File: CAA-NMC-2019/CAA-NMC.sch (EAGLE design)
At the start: 156 parts, among them IC1 ATTINY85-20SU, J1 M20-9980346

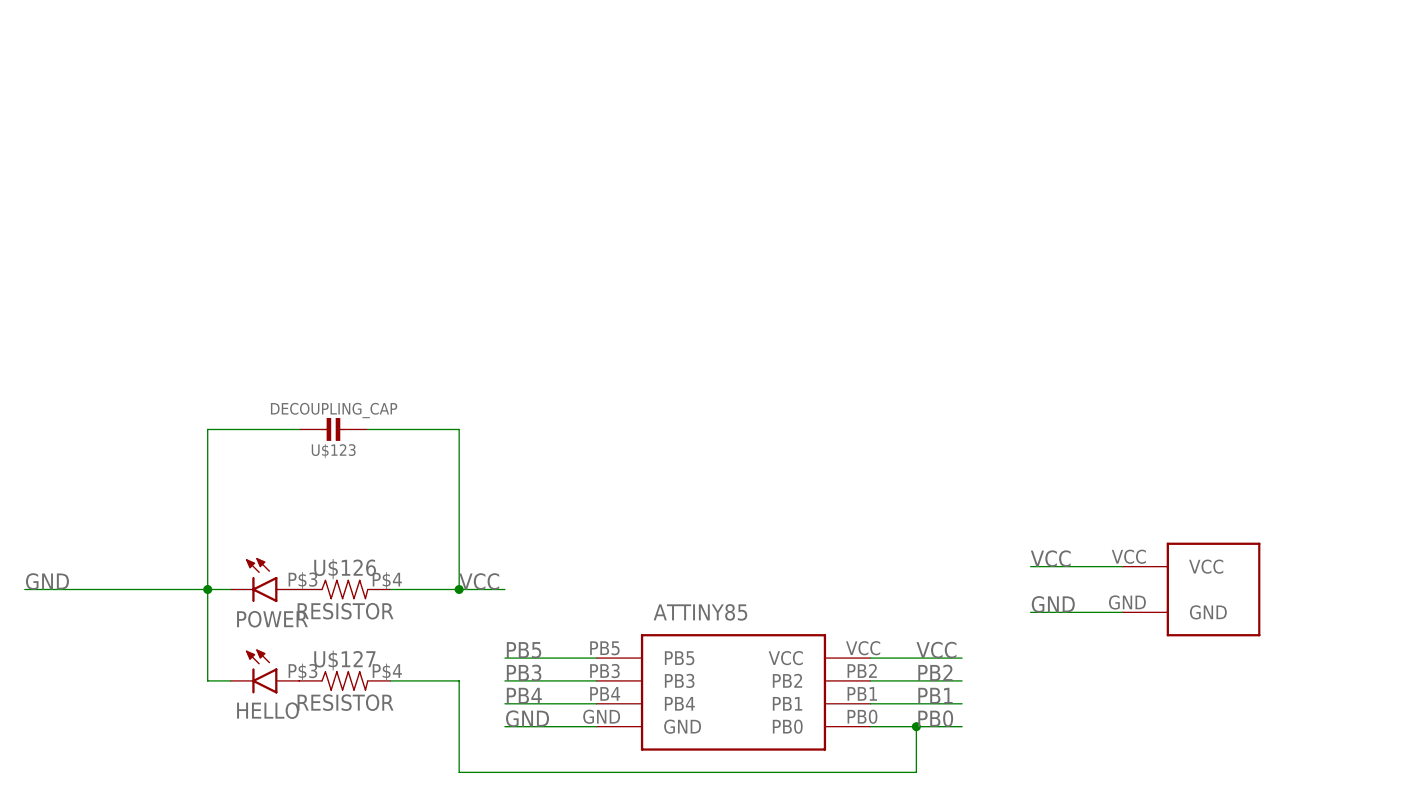
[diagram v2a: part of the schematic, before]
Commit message: added SMT switch to design/lbr
This can be used as on/off for battery, but should also be wired to isolate battery voltage from USB
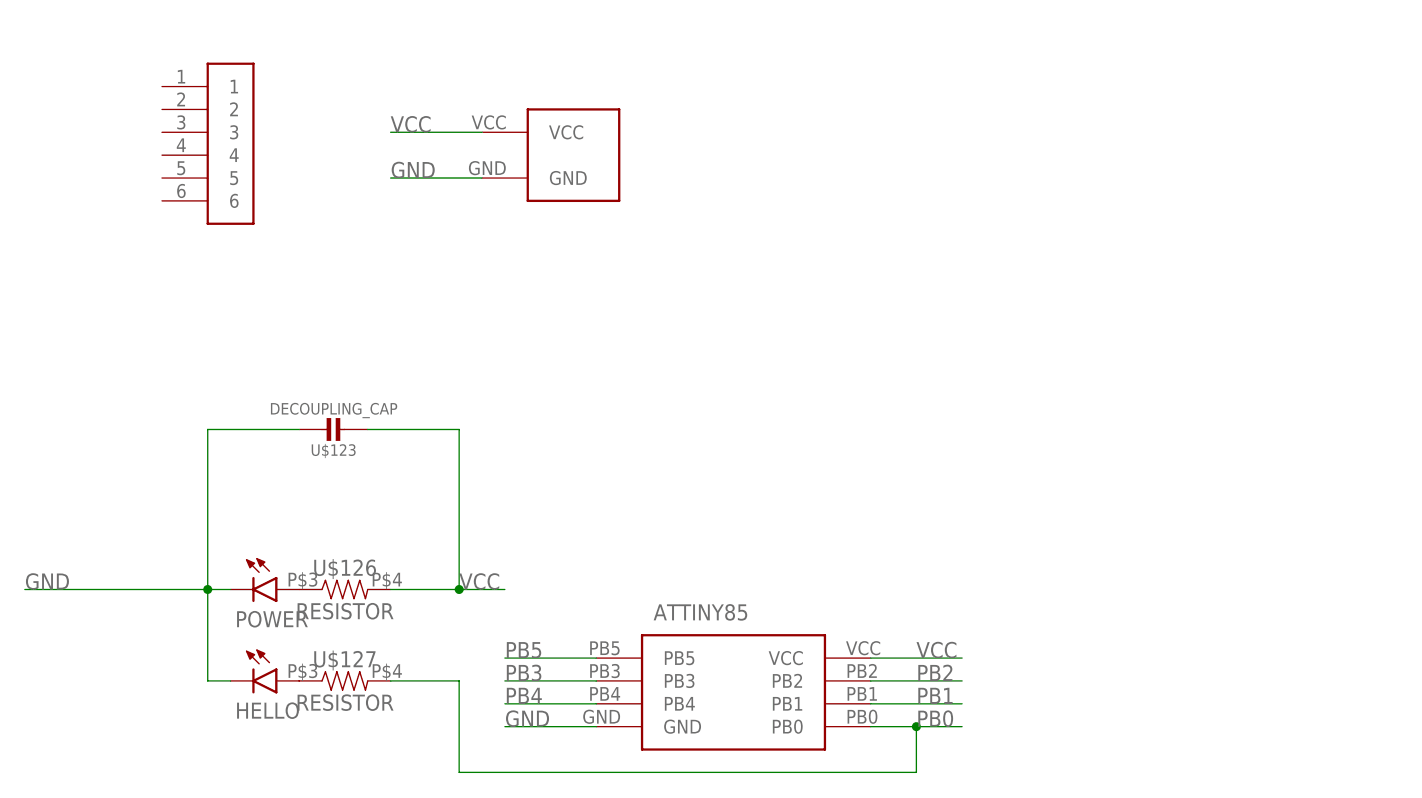
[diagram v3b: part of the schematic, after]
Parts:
- added U$145: SMT-SWITCH, BadgeParts:SMT-SWITCH
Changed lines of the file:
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@@
 <part name="R4" library="SparkFun-Resistors" library_urn="urn:adsk.eagle:library:532" deviceset="10KOHM" device="-0603-1/10W-1%" package3d_urn="urn:adsk.eagle:package:39650/1" value="10k"/>
 <part name="GND5" library="SparkFun-PowerSymbols" library_urn="urn:adsk.eagle:library:530" deviceset="GND" device=""/>
+<part name="U$145" library="BadgeParts" deviceset="SMT-SWITCH" device=""/>
 </parts>
 <sheets>
@@
 <attribute name="VALUE" x="-219.583" y="-82.042" size="1.778" layer="96"/>
 </instance>
-<instance part="U$144" gate="G$1" x="-55.88" y="76.2" smashed="yes"/>
+<instance part="U$144" gate="G$1" x="-127" y="124.46" smashed="yes"/>
 <instance part="LED1" gate="G$1" x="-243.84" y="116.84" smashed="yes">
 <attribute name="NAME" x="-256.54" y="125.222" size="1.778" layer="95"/>
@@
 <attribute name="VALUE" x="-264.16" y="58.166" size="1.778" layer="96" align="top-center"/>
 </instance>
+<instance part="U$145" gate="G$1" x="-162.56" y="129.54" smashed="yes"/>
 </instances>
 <busses>
@@
 <segment>
 <pinref part="U$144" gate="G$1" pin="VCC"/>
-<wire x1="-60.96" y1="76.2" x2="-71.12" y2="76.2" width="0.1524" layer="91"/>
-<label x="-71.12" y="76.2" size="1.778" layer="95"/>
+<wire x1="-132.08" y1="124.46" x2="-142.24" y2="124.46" width="0.1524" layer="91"/>
+<label x="-142.24" y="124.46" size="1.778" layer="95"/>
 </segment>
 </net>
@@
 <segment>
 <pinref part="U$144" gate="G$1" pin="GND"/>
-<wire x1="-60.96" y1="71.12" x2="-71.12" y2="71.12" width="0.1524" layer="91"/>
-<label x="-71.12" y="71.12" size="1.778" layer="95"/>
-</segment>
-<segment>
+<wire x1="-132.08" y1="119.38" x2="-142.24" y2="119.38" width="0.1524" layer="91"/>
+<label x="-142.24" y="119.38" size="1.778" layer="95"/>
+</segment>
+<segment>

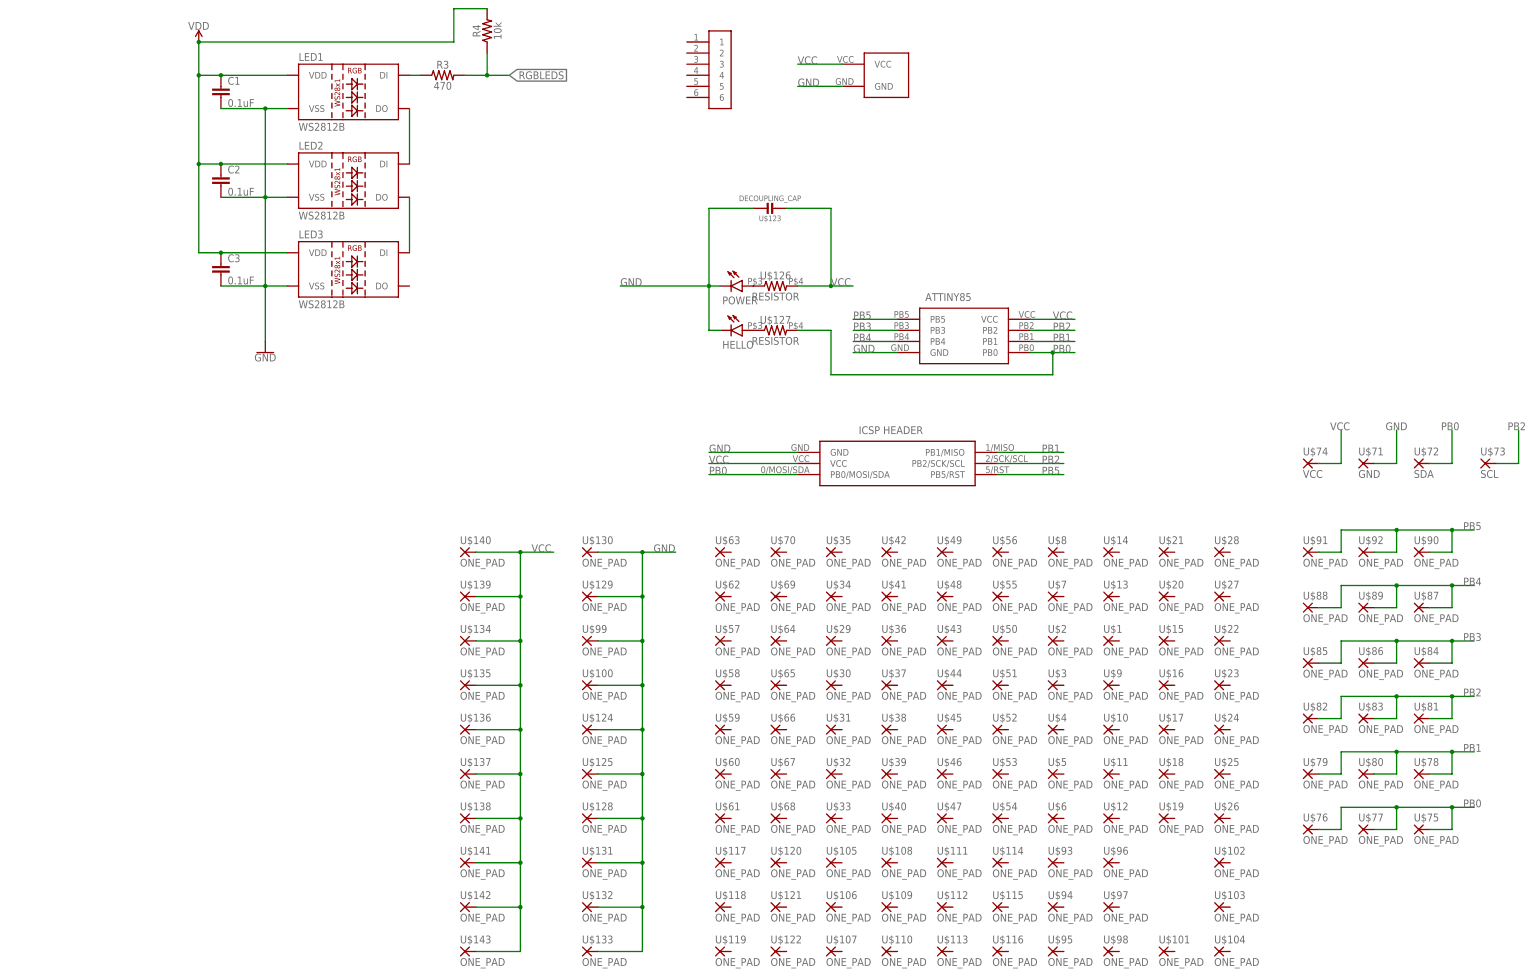
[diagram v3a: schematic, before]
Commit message: updated lbr, proto area simplified
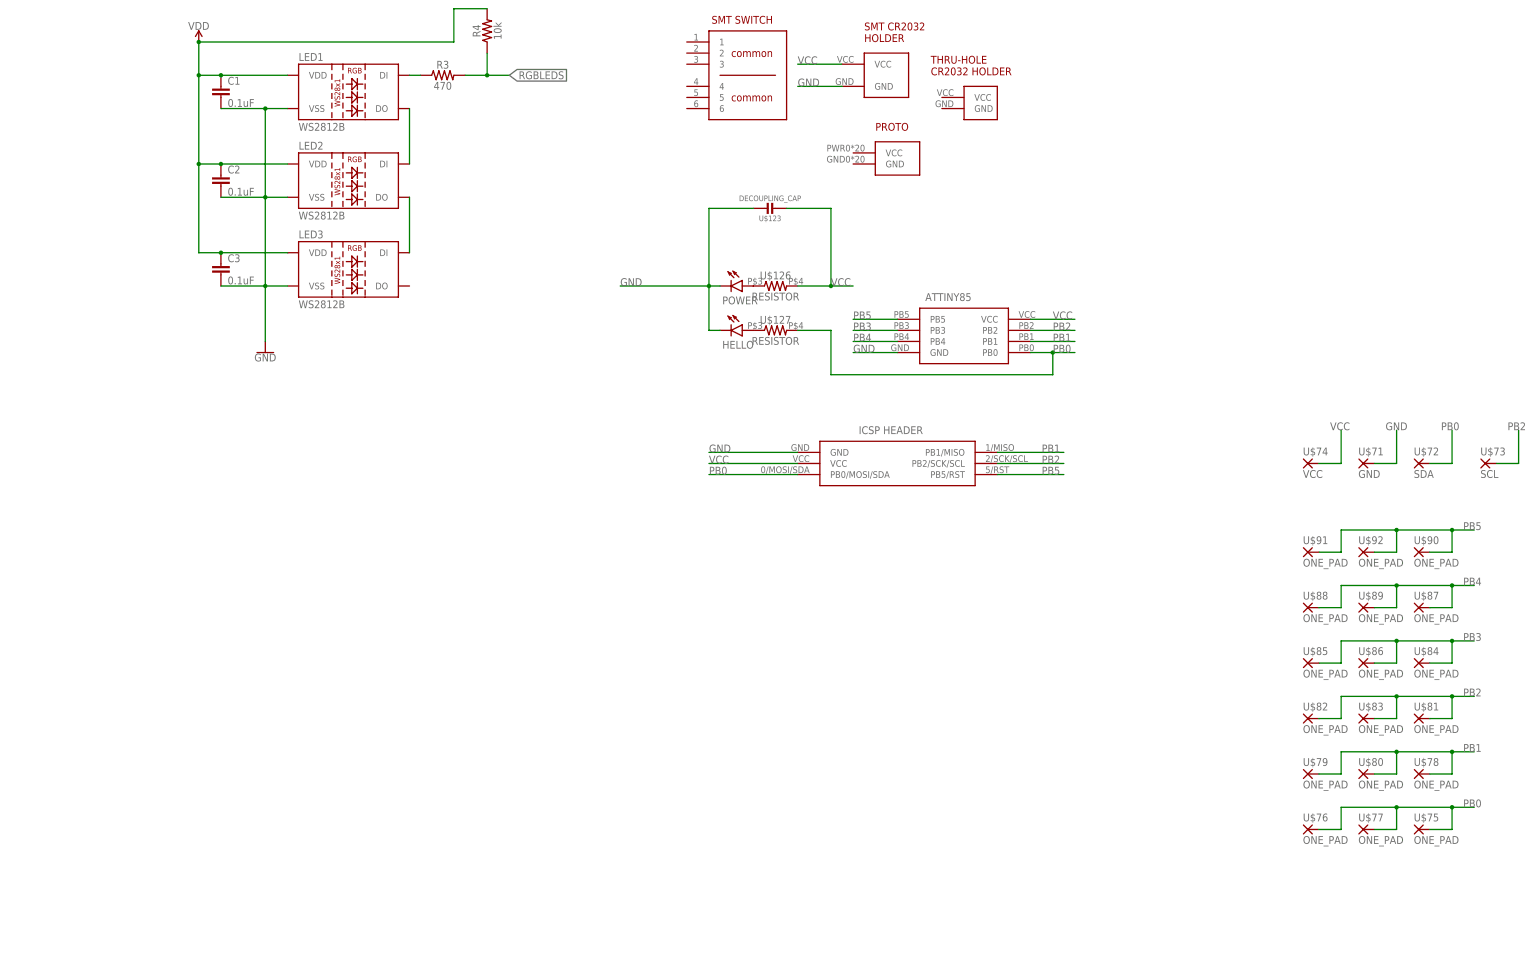
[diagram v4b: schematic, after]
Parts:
- removed U$10, U$100, U$101, U$102, U$103, U$104, U$105, U$106, U$107, U$108, U$109, U$11, U$110, U$111, U$112, U$113, U$114, U$115, U$116, U$117, U$118, U$119, U$12, U$120, U$121, U$122, U$124, U$125, U$128, U$129, U$13, U$130, U$131, U$132, U$133, U$134, U$135, U$136, U$137, U$138, U$139, U$14, U$140, U$141, U$142, U$143, U$15, U$16, U$17, U$18, U$19, U$20, U$21, U$22, U$23, U$24, U$25, U$26, U$27, U$28, U$29, U$3, U$30, U$31, U$32, U$33, U$34, U$35, U$36, U$37, U$38, U$39, U$4, U$40, U$41, U$42, U$43, U$44, U$45, U$46, U$47, U$48, U$49, U$5, U$50, U$51, U$52, U$53, U$54, U$55, U$56, U$57, U$58, U$59, U$6, U$60, U$61, U$62, U$63, U$64, U$65, U$66, U$67, U$68, U$69, U$7, U$70, U$8, U$9, U$93, U$94, U$95, U$96, U$97, U$98, U$99: ONE_PAD, BadgeParts:ONE_PAD
- U$1: value ONE_PAD -> PROTO; device BadgeParts:ONE_PAD -> BadgeParts:PROTO
- U$2: value ONE_PAD -> THRU-CR-HOLDER; device BadgeParts:ONE_PAD -> BadgeParts:THRU-CR-HOLDER
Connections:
- net GND: no longer U$100.P, U$124.P, U$125.P, U$128.P, U$129.P, U$130.P, U$131.P, U$132.P, U$133.P, U$99.P
- net VCC: no longer U$134.P, U$135.P, U$136.P, U$137.P, U$138.P, U$139.P, U$140.P, U$141.P, U$142.P, U$143.P
